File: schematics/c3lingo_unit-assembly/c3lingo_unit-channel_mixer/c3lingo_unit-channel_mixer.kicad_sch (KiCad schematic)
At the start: 93 parts, among them J301 Interconnect, J302 PowerSupply, J303 I/O, Q301 MMBFJ113, SW301 OnAir_X, SW302 Mute_X, U301 TL072, U302 LM339, U303 LM339, U304 LM339, U305 LM833-N

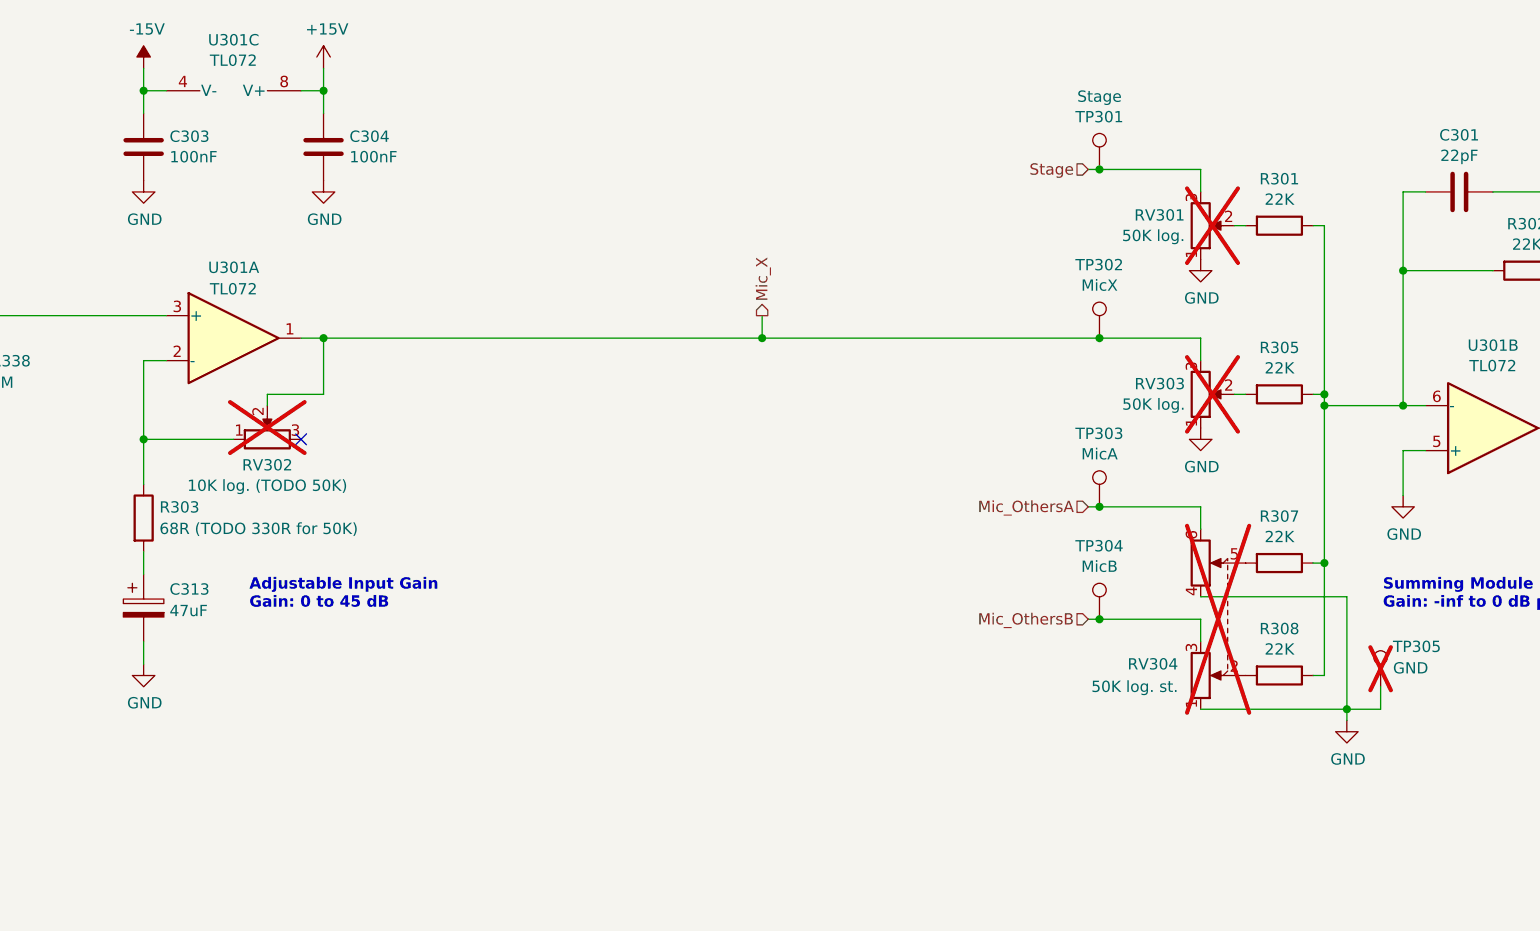
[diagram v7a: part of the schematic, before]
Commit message: Channel: Change to single channel potentiometers
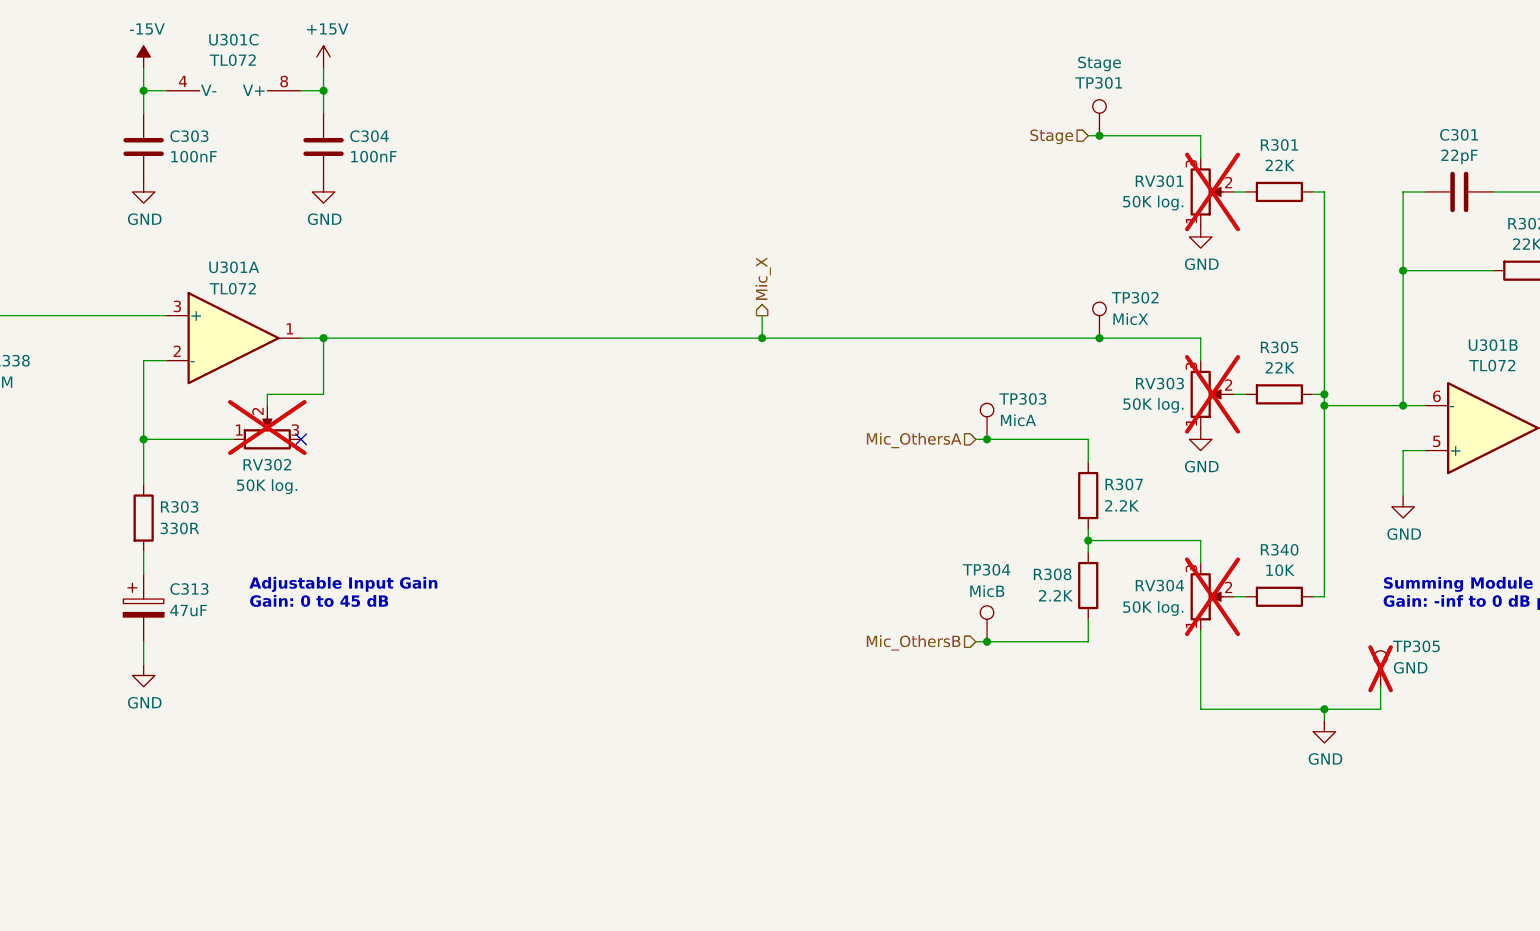
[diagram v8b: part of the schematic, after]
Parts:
- added R340: 10K, Resistor_SMD:R_0805_2012Metric_Pad1.20x1.40mm_HandSolder, symbol Device:R
- R303: value 68R (TODO 330R for 50K) -> 330R
- R307, R308: value 22K -> 2.2K; LCSC Part # C17560 -> (none)
- RV301, RV303: footprint c3lingo_unit-footprints:Potentiometer_Alps_RK09K_Double_Vertical -> c3lingo_unit-footprints:Potentiometer_CUI_PTN09X_Single_Vertical; Model Alps RK09K12C0A2S (dual, vert.) -> CUI Devices PTN091-V50115K1A (single, vert.)
- RV302: value 10K log. (TODO 50K) -> 50K log.; footprint Potentiometer_THT:Potentiometer_Alps_RK09K_Single_Vertical -> c3lingo_unit-footprints:Potentiometer_CUI_PTN09X_Single_Vertical; Model Alps RK09K1130AJ3 (single, vert.) -> CUI Devices PTN091-V50115K1A (single, vert.)
- RV304: value 50K log. st. -> 50K log.; footprint c3lingo_unit-footprints:Potentiometer_Alps_RK09K_Double_Vertical -> c3lingo_unit-footprints:Potentiometer_CUI_PTN09X_Single_Vertical; symbol Device:R_Potentiometer_Dual -> Device:R_Potentiometer; Model Alps RK09K12C0A2S (dual, vert.) -> CUI Devices PTN091-V50115K1A (single, vert.)
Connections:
- net GND: no longer RV304.4
- net Mic_OthersA: now also R307.1; no longer RV304.6
- net Mic_OthersB: now also R308.1; no longer RV304.3
- net at RV304.2: now also R340.2; no longer R308.2
- net at R307.2: now also R308.2, RV304.3; no longer RV304.5
- net at C301.2, R301.1, R302.2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: now also R340.1; no longer R307.1, R308.1
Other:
- moved on the sheet: R301, R307, R308, RV301, TP301, TP303, TP304
